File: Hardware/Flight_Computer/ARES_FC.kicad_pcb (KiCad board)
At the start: 2 copper layers, 57.2 x 57.2 mm, 63 parts, among them J1 SWD, J2 TYPE-C-31-M-12, J3 FC_M/P, J4 5V, J5 GND, J6 FC_RF, U1 STM32F401CCU6, U2 AMS1117-3.3, U3 BMP280, U4 BNO055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

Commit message: routing 99% done
double check external antenna connector. S1 & S2 unused for ribbons. DRC not completed.
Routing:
- net +3.3V: track 150.0 -> 235.6 mm, vias 8 -> 11
- net VBUS: track 71.0 -> 126.5 mm, vias 0 -> 2
- net /RADIO_NRST: track 0.00 -> 40.2 mm, vias 0 -> 2
- net /MOTOR_NRST: track 0.00 -> 30.9 mm, vias 0 -> 2
- net /BNO_NRST: track 6.37 -> 30.5 mm, vias 1 -> 2
- net /SWCLK: track 26.7 -> 46.4 mm
- net /LED_G: track 11.6 -> 21.9 mm
- net /SCL: track 25.6 -> 34.6 mm, vias 2 -> 3
- net /SDA: track 25.8 -> 34.4 mm, vias 0 -> 2
- net GND: track 135.3 -> 128.5 mm, vias 25 -> 28
- net Net-(J2-CC1): track 0.00 -> 2.11 mm
- net /MOSI: track 14.1 -> 15.8 mm
- net /CS_FLASH: track 29.6 -> 30.9 mm
- net /SCLK: track 17.8 -> 19.0 mm
- net /MISO: track 25.0 -> 26.2 mm
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- added copper zone on B.Cu, net GND
- added copper zone on F.Cu, net GND
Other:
- board text removed: "CIRCLE CENTER"

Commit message: DRC fixes
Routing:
- net GND: track 128.5 -> 132.5 mm
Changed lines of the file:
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@@
+	)
+	(segment
+		(start 141.5548 90.31134)
+		(end 141.5548 90.1452)
+		(width 0.25)
+		(layer "F.Cu")
+		(net 2)
 	)
 	(segment
@@
 	)
 	(segment
+		(start 128.8925 92.3595)
+		(end 128.4125 91.8795)
+		(width 0.25)
+		(layer "F.Cu")
+		(net 2)
+	)
+	(segment
 		(start 137.9108 92.90734)
 		(end 136.40734 92.90734)
@@
 	)
 	(segment
+		(start 141.5548 90.1452)
+		(end 143.35146 88.34854)
+		(width 0.25)
+		(layer "F.Cu")
+		(net 2)
+	)
+	(segment
 		(start 128.8925 92.3595)
 		(end 127.7506 92.3595)
@@
 	)
 	(segment
+		(start 128.4125 90.3375)
+		(end 128.275 90.2)
+		(width 0.25)
+		(layer "F.Cu")
+		(net 2)
+	)
+	(segment
 		(start 158.45 104.15)
 		(end 159.55 104.15)
@@
 	)
 	(segment
+		(start 128.4125 91.6976)
+		(end 127.7193 92.3908)
+		(width 0.25)
+		(layer "F.Cu")
+		(net 2)
+	)
+	(segment
 		(start 150.6 92.04974)
 		(end 148.35 89.79974)
@@
 	)
 	(segment
+		(start 128.4125 91.1125)
+		(end 128.4125 90.3375)
+		(width 0.25)
+		(layer "F.Cu")
+		(net 2)
+	)
+	(segment
 		(start 134.05 89.7)
 		(end 133.05 89.7)
@@
 	)
 	(segment
-		(start 143.378 88.48814)
+		(start 143.35146 88.34854)
 		(end 143.378 88.34854)
 		(width 0.25)
@@
 	)
 	(segment
+		(start 128.4125 91.8795)
+		(end 128.4125 91.1125)
+		(width 0.25)
+		(layer "F.Cu")
+		(net 2)
+	)
+	(segment
 		(start 144.5 113.15)
 		(end 143.55 113.15)
@@
 	)
 	(segment
+		(start 128.4125 91.1125)
+		(end 128.4125 91.6976)
+		(width 0.25)
+		(layer "F.Cu")
+		(net 2)
+	)
+	(segment
 		(start 158.550001 114.65)
 		(end 157.05 113.149999)
@@
 	)
 	(segment
-		(start 141.5548 90.31134)
-		(end 143.378 88.48814)
-		(width 0.25)
-		(layer "F.Cu")
-		(net 2)
-	)
-	(segment
 		(start 145.086 93.99254)
 		(end 145.086 93.94054)
@@
 	)
 	(via
-		(at 143.23875 89.26104)
-		(size 0.8)
-		(drill 0.4)
+		(at 143.378 88.34854)
+		(size 0.8)
+		(drill 0.4)

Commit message: Antenna and Model Changes Added Fencing Vias to Ext. GPS Antenna Added 3D Models for Ribbon Connectors and GPS
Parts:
- moved G*** 38.9 mm to (149.6, 84.6)
- moved AE1 2.94 mm to (172.5, 113.8)
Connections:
- J3 pad 3: /S1 -> /S1_MP
- J3 pad 4: /S2 -> /S2_MP
- J6 pad 3: /S1 -> /S1_RF
- J6 pad 4: /S2 -> /S2_RF
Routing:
- net VBUS: track 126.5 -> 135.1 mm
- net Net-(AE1-A): track 16.0 -> 14.5 mm, vias 2 -> 0
- net GND: vias 28 -> 65
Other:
- board text added: "ARES V2 Society For Advanced Rocket Propulsion"
- board text removed: "Reaction Control System Society For Advanced Rocket Propulsion"

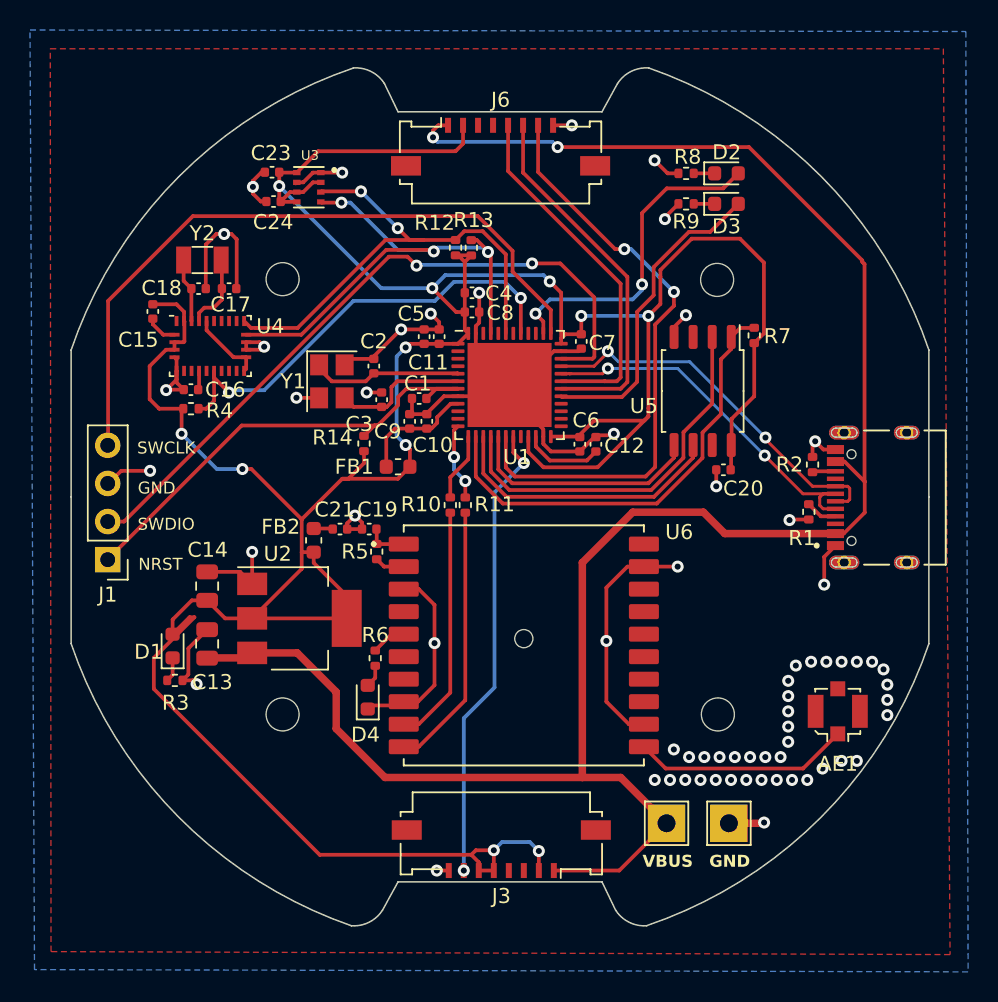
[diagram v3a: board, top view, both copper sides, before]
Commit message: fixed ribbon connectors and S1 & S2
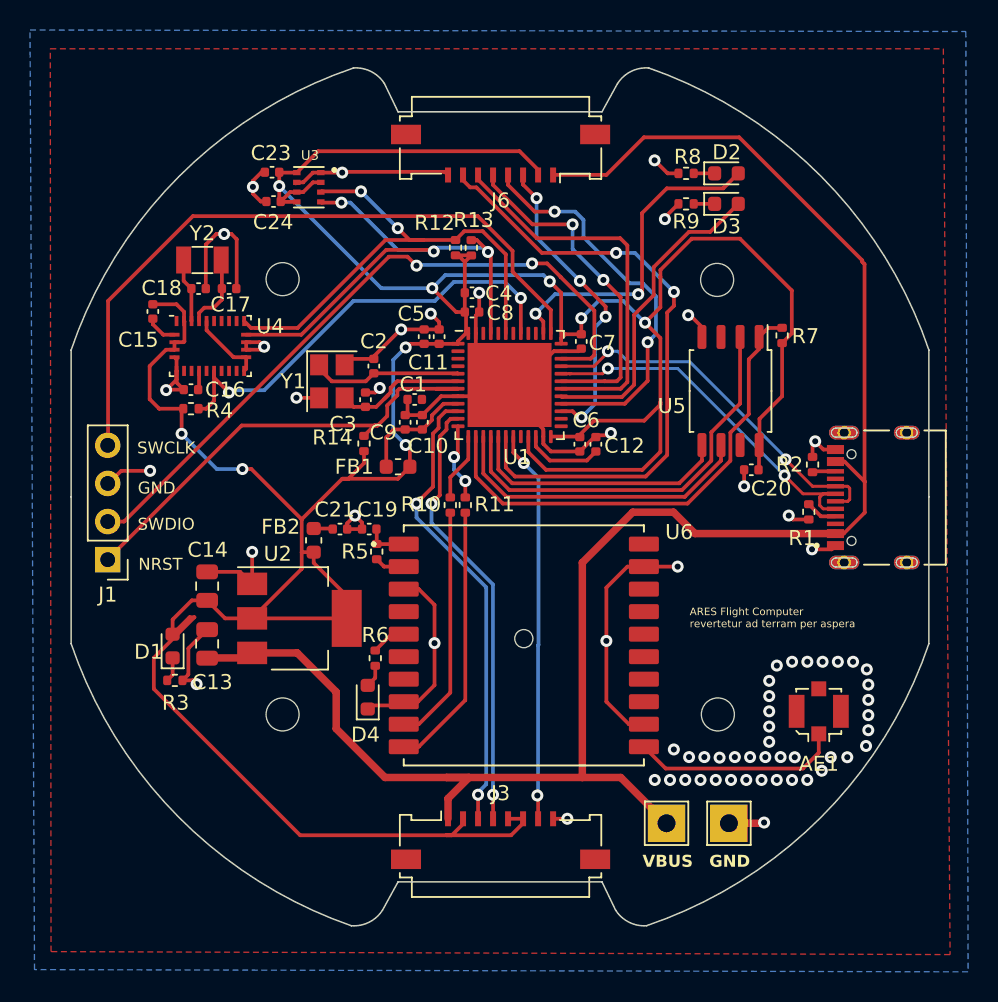
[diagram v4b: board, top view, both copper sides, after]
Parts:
- moved G*** 15.4 mm to (149.6, 100.0)
- moved C20 1.86 mm to (166.7, 97.7)
- moved R7 1.86 mm to (168.8, 88.8)
- moved U5 1.86 mm to (165.3, 92.5)
- moved J3 1.63 mm to (150.0, 121.9), turned to 0 degrees
- moved J6 1.49 mm to (150.0, 77.2), turned to 180 degrees
- moved AE1 1.27 mm to (171.2, 113.8)
- moved C3 1.08 mm to (141.0, 93.0)
- moved C1 0.30 mm to (144.3, 93.0)
- moved C10 0.30 mm to (144.8, 94.5)
- moved C9 0.30 mm to (143.6, 94.5)
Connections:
- U1 pad 10: unconnected-(U1-PA0-Pad10) -> /S1_MP
- U1 pad 11: unconnected-(U1-PA1-Pad11) -> /S2_MP
- U1 pad 27: unconnected-(U1-PB14-Pad27) -> /S1_RF
- U1 pad 28: unconnected-(U1-PB15-Pad28) -> /S2_RF
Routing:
- net /S1_MP: track 0.00 -> 30.9 mm, vias 0 -> 2
- net /S2_MP: track 0.00 -> 29.4 mm, vias 0 -> 2
- net /S2_RF: track 0.00 -> 26.5 mm, vias 0 -> 2
- net /S1_RF: track 0.00 -> 20.6 mm, vias 0 -> 4
- net VBUS: track 135.1 -> 122.5 mm, vias 2 -> 0
- net +3.3V: track 235.6 -> 241.8 mm, vias 11 -> 9
- net /MOTOR_NRST: track 30.9 -> 26.2 mm
- net GND: track 132.5 -> 137.0 mm, vias 65 -> 67
- net /RADIO_NRST: track 40.2 -> 42.2 mm
- net /MOSI: track 15.8 -> 17.8 mm
- net /SCLK: track 19.0 -> 21.0 mm
- net /CS_FLASH: track 30.9 -> 32.4 mm
- net /RX_RADIO: track 24.0 -> 22.6 mm, vias 0 -> 2
- net /TX_RADIO: track 24.6 -> 25.8 mm
- net /MISO: track 26.2 -> 27.4 mm
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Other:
- board text added: "ARES Flight Computer revertetur ad terram per aspera"
- board text removed: "CIRCLE EDGE"

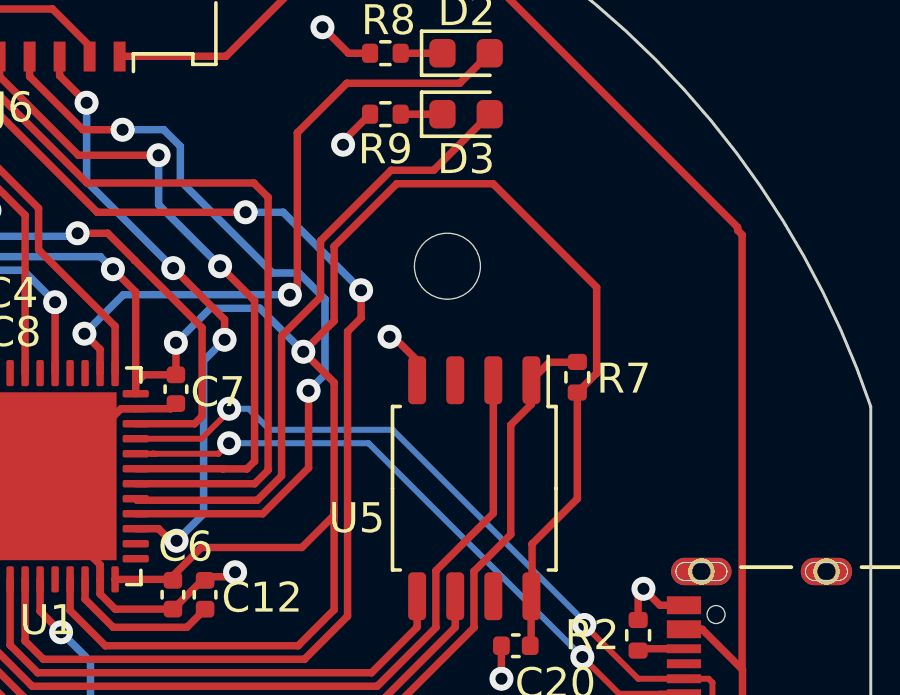
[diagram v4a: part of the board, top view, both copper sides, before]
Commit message: tiny routing change for aesthetic purposes
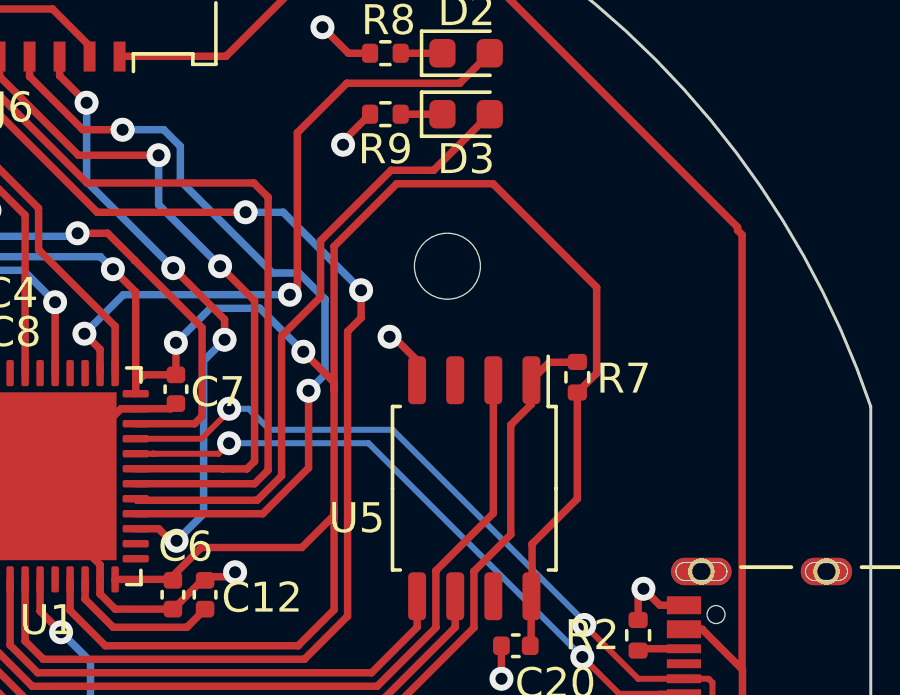
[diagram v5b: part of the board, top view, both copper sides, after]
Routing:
- net +3.3V: track 241.8 -> 242.7 mm
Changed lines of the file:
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@@
 		(tags "connector Molex  top entry")
 		(property "Reference" "J3"
-			(at 0 -2.61 360)
+			(at 0 -2.61 0)
 			(layer "F.SilkS")
 			(effects
@@
 		)
 		(property "Value" "FC_M/P"
-			(at 0 5.39 360)
+			(at 0 5.39 0)
 			(layer "F.Fab")
 			(effects
@@
 		)
 		(fp_text user "${REFERENCE}"
-			(at 0 1.39 360)
+			(at 0 1.39 0)
 			(layer "F.Fab")
 			(effects
@@
 		(tags "connector Molex  top entry")
 		(property "Reference" "J6"
-			(at 0 -2.61 360)
+			(at 0 -2.61 0)
 			(layer "F.SilkS")
 			(effects
@@
 		)
 		(property "Value" "FC_RF"
-			(at 0 5.39 360)
+			(at 0 5.39 0)
 			(layer "F.Fab")
 			(effects
@@
 		)
 		(fp_text user "${REFERENCE}"
-			(at 0 1.39 360)
+			(at 0 1.39 0)
 			(layer "F.Fab")
 			(effects
@@
 	)
 	(segment
-		(start 160.65 88.925)
-		(end 160.65 93.2)
-		(width 0.25)
-		(layer "F.Cu")
-		(net 5)
-	)
-	(segment
 		(start 143.678 96.04854)
 		(end 143.9595 96.33004)
@@
 	)
 	(segment
-		(start 165.95 82.3)
-		(end 169.4025 85.7525)
-		(width 0.25)
-		(layer "F.Cu")
-		(net 5)
-	)
-	(segment
 		(start 147.5 121.3)
 		(end 147.5 120.95)
@@
 	)
 	(segment
+		(start 160.64927 89.14927)
+		(end 160.65 89.15)
+		(width 0.25)
+		(layer "F.Cu")
+		(net 5)
+	)
+	(segment
+		(start 162.736396 82.3)
+		(end 160.65 84.386396)
+		(width 0.25)
+		(layer "F.Cu")
+		(net 5)
+	)
+	(segment
 		(start 128.9125 87.7875)
 		(end 128.9375 87.8125)
@@
 	)
 	(segment
+		(start 165.95 82.3)
+		(end 162.736396 82.3)
+		(width 0.25)
+		(layer "F.Cu")
+		(net 5)
+	)
+	(segment
 		(start 147.03974 87.18974)
 		(end 147.617 87.18974)
@@
 	)
 	(segment
-		(start 160.64927 86.87573)
-		(end 160.64927 84.85073)
-		(width 0.25)
-		(layer "F.Cu")
-		(net 5)
-	)
-	(segment
 		(start 147.617 85.90674)
 		(end 147.617 83.853)
@@
 	)
 	(segment
-		(start 169.4025 85.7525)
-		(end 169.4025 88.615)
-		(width 0.25)
-		(layer "F.Cu")
-		(net 5)
-	)
-	(segment
 		(start 140.9 96.46)
 		(end 140.9 97.26208)
@@
 	)
 	(segment
+		(start 168.7575 89.26)
+		(end 169.4025 88.615)
+		(width 0.25)
+		(layer "F.Cu")
+		(net 5)
+	)
+	(segment
 		(start 167.249148 94.308352)
 		(end 168.7575 92.8)
@@
 	)
 	(segment
-		(start 160.65 84.386396)
-		(end 162.736396 82.3)
-		(width 0.25)
-		(layer "F.Cu")
-		(net 5)
-	)
-	(segment
 		(start 153.278 85.14854)
 		(end 154.0375 85.90804)
@@
 	)
 	(segment
-		(start 169.4025 88.615)
-		(end 168.7575 89.26)
+		(start 169.4025 85.7525)
+		(end 165.95 82.3)
 		(width 0.25)
 		(layer "F.Cu")
@@
 	)
 	(segment
-		(start 137.85 76.475)
-		(end 136.425 77.9)
+		(start 160.65 84.386396)
+		(end 160.65 84.85)
 		(width 0.25)
 		(layer "F.Cu")
@@
 	)
 	(segment
-		(start 133.45 107.6)
-		(end 131.65 107.6)
+		(start 137.85 76.475)
+		(end 136.425 77.9)
 		(width 0.25)
 		(layer "F.Cu")
@@
 	)
 	(segment
-		(start 162.736396 82.3)
-		(end 165.95 82.3)
+		(start 133.45 107.6)
+		(end 131.65 107.6)
 		(width 0.25)
 		(layer "F.Cu")
@@
 	)
 	(segment
+		(start 169.4025 88.615)
+		(end 169.4025 85.7525)
+		(width 0.25)
+		(layer "F.Cu")
+		(net 5)
+	)
+	(segment
 		(start 137.55 103.1875)
 		(end 137.55 103.9)
@@
 	)
 	(segment
+		(start 160.64927 84.85073)
+		(end 160.64927 89.14927)
+		(width 0.25)
+		(layer "F.Cu")
+		(net 5)
+	)
+	(segment
 		(start 127.714 89.7)
 		(end 126.6193 90.7947)
@@
 	)
 	(segment
-		(start 144.91 89.30774)
-		(end 143.9188 89.30774)
+		(start 160.65 89.15)
+		(end 160.65 93.2)
 		(width 0.25)
 		(layer "F.Cu")
@@
 	)
 	(segment
-		(start 160.64927 84.85073)
-		(end 160.65 84.85)
+		(start 144.91 89.30774)
+		(end 143.9188 89.30774)
 		(width 0.25)
 		(layer "F.Cu")
@@
 	)
 	(segment
+		(start 160.65 84.85)
+		(end 160.64927 84.85073)
+		(width 0.25)
+		(layer "F.Cu")
+		(net 5)
+	)
+	(segment
 		(start 139.75 107.4295)
 		(end 139.75 107.6)
@@
 	)
 	(segment
+		(start 160.65 88.925)
+		(end 160.65 89.15)
+		(width 0.25)
+		(layer "F.Cu")
+		(net 5)
+	)
+	(segment
 		(start 136.75 104.3)
 		(end 136.75 103.2)
@@
 	)
 	(segment
-		(start 159.625 87.9)
-		(end 160.64927 86.87573)
-		(width 0.25)
-		(layer "F.Cu")
-		(net 5)
-	)
-	(segment
 		(start 126.9 110.22946)
 		(end 126.9 112.3)
@@
 		(width 0.25)
 		(layer "F.Cu")
-		(net 5)
-	)
-	(segment
-		(start 160.65 84.85)
-		(end 160.65 84.386396)
-		(width 0.25)
-		(layer "F.Cu")
